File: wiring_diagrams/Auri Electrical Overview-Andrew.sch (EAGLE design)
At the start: 62 parts, among them T1 2N7002E, T2 2N7002E, T3 2N7002E, T4 2N7002E, T5 2N7002E, U1 LTV-355T, U2 LTV-355T, U3 LTV-355T, U4 LTV-355T, U5 LTV-355T

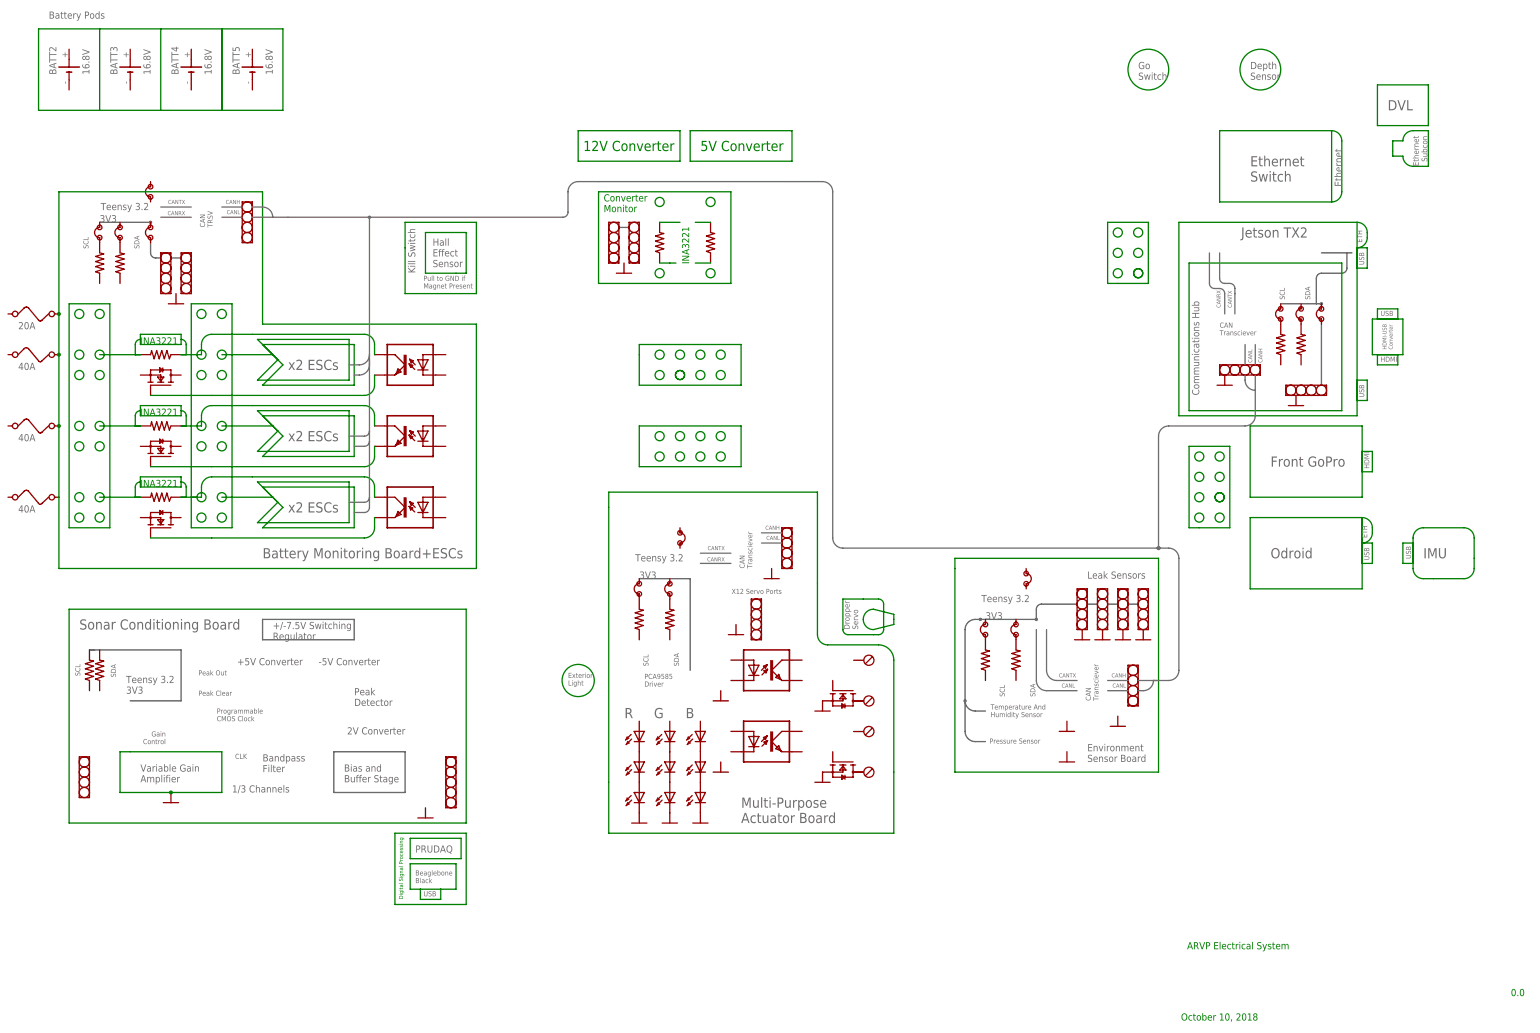
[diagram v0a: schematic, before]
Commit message: Modified electrical overview
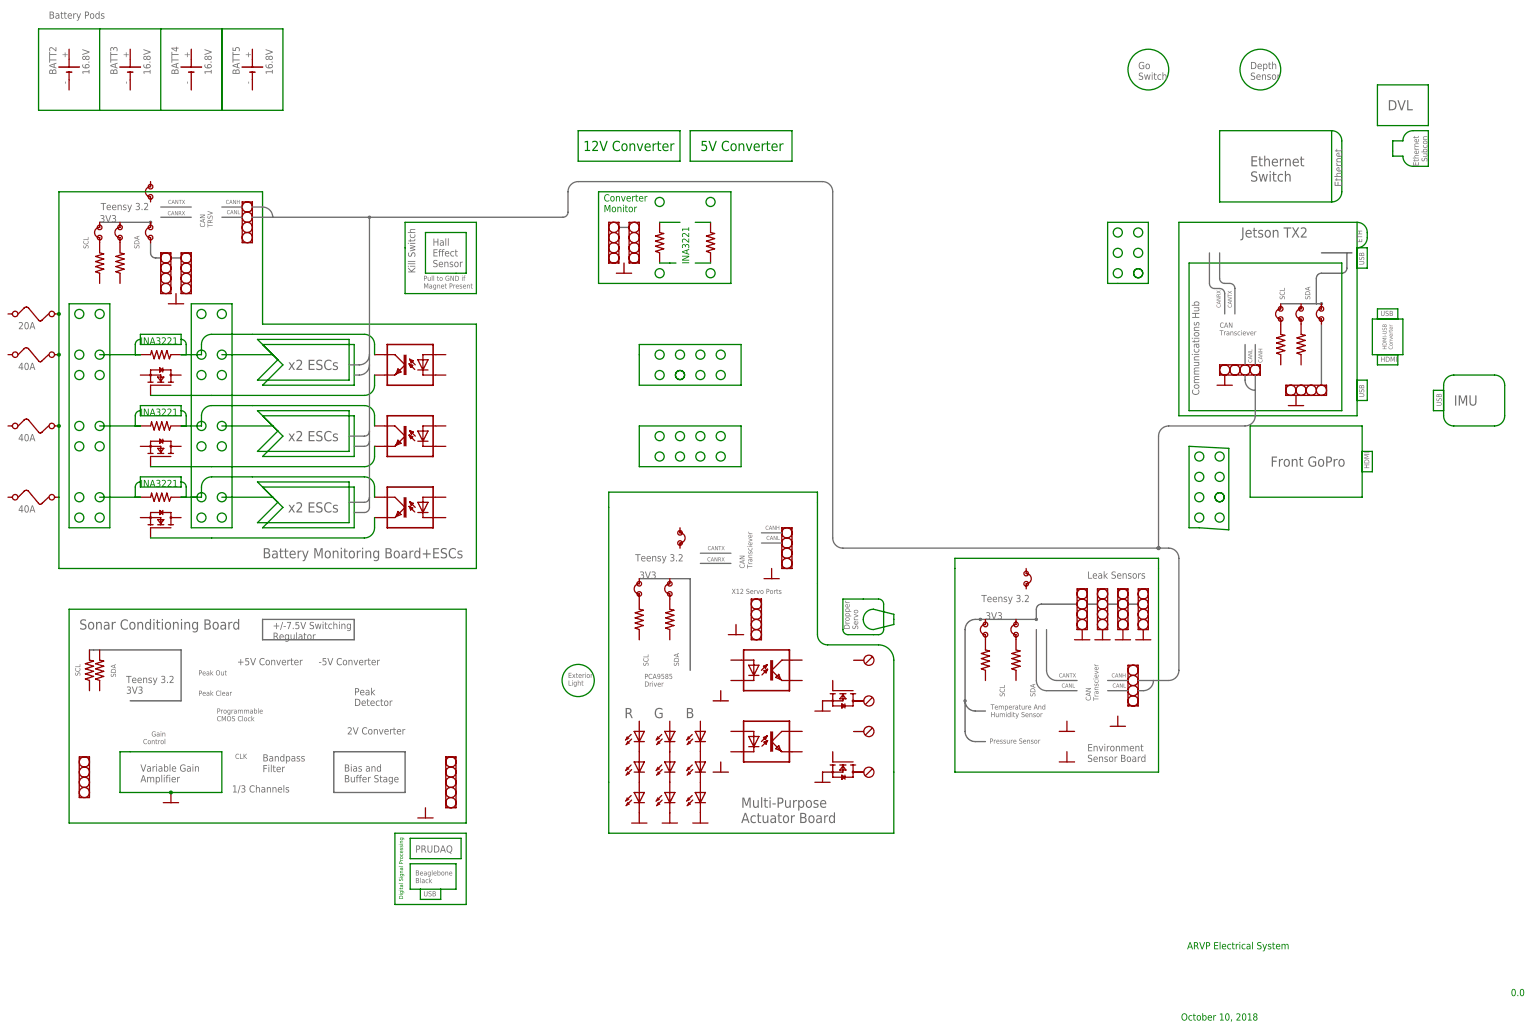
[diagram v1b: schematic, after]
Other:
- note removed: "Odroid"
